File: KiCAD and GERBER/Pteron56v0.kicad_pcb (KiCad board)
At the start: 2 copper layers, 293.7 x 154 mm, 135 parts, among them SW1 SW_PUSH, SW10 SW_PUSH, SW11 SW_PUSH, SW12 SW_PUSH, SW13 SW_PUSH, SW14 SW_PUSH, SW15 SW_PUSH, SW16 SW_PUSH, SW17 SW_PUSH, SW18 SW_PUSH, SW19 SW_PUSH, SW2 SW_PUSH, SW20 SW_PUSH, SW21 SW_PUSH, SW22 SW_PUSH, SW23 SW_PUSH, SW24 SW_PUSH, SW25 SW_PUSH, SW26 SW_PUSH, SW27 SW_PUSH, SW28 SW_PUSH, SW29 SW_PUSH, SW3 SW_PUSH, SW30 SW_PUSH, SW31 SW_PUSH, SW32 SW_PUSH, SW33 SW_PUSH, SW34 SW_PUSH, SW35 SW_PUSH, SW36 SW_PUSH, SW37 SW_PUSH, SW38 SW_PUSH, SW39 SW_PUSH, SW4 SW_PUSH, SW40 SW_PUSH, SW41 SW_PUSH, SW42 SW_PUSH, SW43 SW_PUSH, SW44 SW_PUSH, SW45 SW_PUSH, SW46 SW_PUSH, SW47 SW_PUSH, SW48 SW_PUSH, SW49 SW_PUSH, SW5 SW_PUSH, SW50 SW_PUSH, SW51 SW_PUSH, SW52 SW_PUSH, SW53 SW_PUSH, SW54 SW_PUSH, SW55 SW_PUSH, SW56 SW_PUSH, SW6 SW_PUSH, SW7 SW_PUSH, SW8 SW_PUSH, SW9 SW_PUSH, U1 ProMicro

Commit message: add split wiring for standard Pteron56v0
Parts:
- removed D29, D30, D31, D32, D33, D34, D35, D36, D37, D38, D39, D40, D41, D42, D43, D44, D45, D46, D47, D48, D49, D50, D51, D52, D53, D54, D55, D56: 1N4148, Keyboard parts:D_DO-35_SOD27_P7.62mm_Horizontal
- removed G*** (x2): LOGO, Logos:PTERONsmaller
- removed G*** (x2): LOGO, Logos:bat56
- removed REF** (x18): MountingHole_2mm, MountingHole:MountingHole_2mm
- removed SW29, SW30, SW31, SW32, SW33, SW34, SW35, SW36, SW37, SW38, SW39, SW40, SW41, SW42, SW43, SW44, SW45, SW46, SW47, SW48, SW49, SW50, SW51, SW52, SW53, SW54, SW55, SW56: SW_PUSH, Keyboard parts:Mx_Alps_100
- added J1: AudioJack4, Connector_Audio:Jack_3.5mm_PJ320D_Horizontal, F.Cu at (105.9, 31.2)
- added J2: AudioJack4, Connector_Audio:Jack_3.5mm_PJ320D_Horizontal, B.Cu at (105.9, 31.2)
- D1, D10, D11, D12, D13, D14, D15, D16, D17, D18, D19, D2, D20, D21, D22, D23, D24, D25, D26, D27, D28, D3, D4, D5, D6, D7, D8, D9: footprint Keyboard parts:D_DO-35_SOD27_P7.62mm_Horizontal -> Keebio-Parts:Diode-dual
- SW1, SW10, SW11, SW12, SW13, SW14, SW15, SW16, SW17, SW18, SW19, SW2, SW20, SW21, SW22, SW23, SW24, SW25, SW26, SW27, SW28, SW3, SW4, SW5, SW6, SW7, SW8, SW9: footprint Keyboard parts:Mx_Alps_100 -> Keebio-Parts:Hybrid_PCB_100H_Dual_hole
- U1: footprint Keyboard parts:Pro_Micro -> promicro:ProMicro
- moved SW20 89.6 mm to (87.1, 128.9), turned to 37.5 degrees
- moved U1 86.9 mm to (159.5, 32.5)
- moved SW15 85.0 mm to (104.6, 118.4), turned to 25 degrees
- moved SW10 81.2 mm to (123.9, 111.7), turned to 12.5 degrees
- moved D28 78.8 mm to (112.0, 95.3), turned to 90 degrees
- moved SW5 78.5 mm to (144.2, 109.4), turned to 0 degrees
- moved SW28 76.7 mm to (121.5, 91.2), turned to 0 degrees
- moved D24 76.2 mm to (131.0, 93.9), turned to 90 degrees
- moved D5 76.0 mm to (165.8, 106.8), turned to 90 degrees
- moved D10 75.7 mm to (169.7, 106.8), turned to 90 degrees
- moved D15 75.4 mm to (173.6, 106.8), turned to 90 degrees
- moved D20 75.1 mm to (177.7, 106.8), turned to 90 degrees
- moved D27 74.5 mm to (111.9, 76.5), turned to 90 degrees
- moved SW24 74.0 mm to (140.5, 89.2), turned to 0 degrees
- moved D9 73.0 mm to (187.9, 101.2), turned to 90 degrees
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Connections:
- U1 pad 1: /Row0 -> (no net)
- U1 pad 10: /Col11 -> /Row2
- U1 pad 11: /Col10 -> /Row3
- U1 pad 19: Net-(U1-Pad19) -> (no net)
- U1 pad 2: /Row1 -> (no net)
- U1 pad 20: /Row2 -> (no net)
- U1 pad 21: Net-(U1-Pad21) -> (no net)
- U1 pad 22: Net-(U1-Pad22) -> (no net)
- U1 pad 23: Net-(U1-Pad23) -> (no net)
- U1 pad 24: Net-(U1-Pad24) -> (no net)
- U1 pad 3: Net-(U1-Pad3) -> (no net)
- U1 pad 4: Net-(U1-Pad4) -> (no net)
- U1 pad 5: /Col6 -> /Serial
- U1 pad 6: /Col7 -> (no net)
- U1 pad 7: /Row3 -> (no net)
- U1 pad 8: /Col8 -> /Row0
- U1 pad 9: /Col9 -> /Row1
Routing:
- net /Row1: track 403.7 -> 113.4 mm, vias 1 -> 0
- net /Row3: track 405.7 -> 146.7 mm, vias 2 -> 1
- net /Row0: track 377.4 -> 122.7 mm, vias 1 -> 0
- net /Row2: track 368.5 -> 135.1 mm, vias 0 -> 1
- net /Col11: track 202.1 -> 0.00 mm
- net /Col9: track 198.3 -> 0.00 mm, vias 1 -> 0
- net /Col8: track 190.0 -> 0.00 mm
- net /Col10: track 182.8 -> 0.00 mm
- net Net-(D41-Pad2): track 113.1 -> 0.00 mm
- net /Col7: track 112.5 -> 0.00 mm
- net /Col2: track 179.9 -> 83.0 mm, vias 1 -> 0
- net /Col6: track 86.7 -> 0.00 mm
- net Net-(D46-Pad2): track 85.3 -> 0.00 mm
- net /Row4: track 214.7 -> 137.8 mm, vias 0 -> 1
- net /Serial: track 0.00 -> 60.0 mm, vias 0 -> 1
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- added copper zone on B.Cu, net GND
- added copper zone on F.Cu, net VCC
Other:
- board size 293.7 x 154 mm -> 152.4 x 125.7 mm

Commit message: split36 version
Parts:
- removed D1, D2, D3, D4, D5: 1N4148, Keebio-Parts:Diode-dual
- removed SW1, SW2, SW3, SW4, SW5: SW_PUSH, Keebio-Parts:Hybrid_PCB_100H_Dual_hole
- moved D20 90.4 mm to (91.8, 135.1), turned to 217.5 degrees
- moved D15 68.0 mm to (108.2, 125.3), turned to 205 degrees
- moved D10 45.1 mm to (126.4, 119.5), turned to 192.5 degrees
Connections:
- U1 pad 14: /Col0 -> (no net)
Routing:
- net /Col0: track 163.0 -> 0.00 mm, vias 1 -> 0
- net Net-(D20-Pad2): track 102.6 -> 13.1 mm
- net /Col1: track 117.2 -> 191.9 mm
- net /Col2: track 83.0 -> 152.0 mm
- net Net-(D15-Pad2): track 79.8 -> 13.8 mm
- net /Col3: track 148.1 -> 191.5 mm
- net Net-(D10-Pad2): track 54.3 -> 12.7 mm
- net Net-(D5-Pad2): track 29.6 -> 0.00 mm
- net /Row3: track 146.7 -> 121.2 mm
- net /Row2: track 135.1 -> 111.3 mm
- net /Row1: track 113.4 -> 91.2 mm
- net /Row0: track 122.7 -> 104.9 mm
- net Net-(D4-Pad2): track 14.2 -> 0.00 mm
- net Net-(D1-Pad2): track 13.9 -> 0.00 mm
- net Net-(D2-Pad2): track 13.9 -> 0.00 mm
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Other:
- board size 152.4 x 125.7 mm -> 133.3 x 125.7 mm

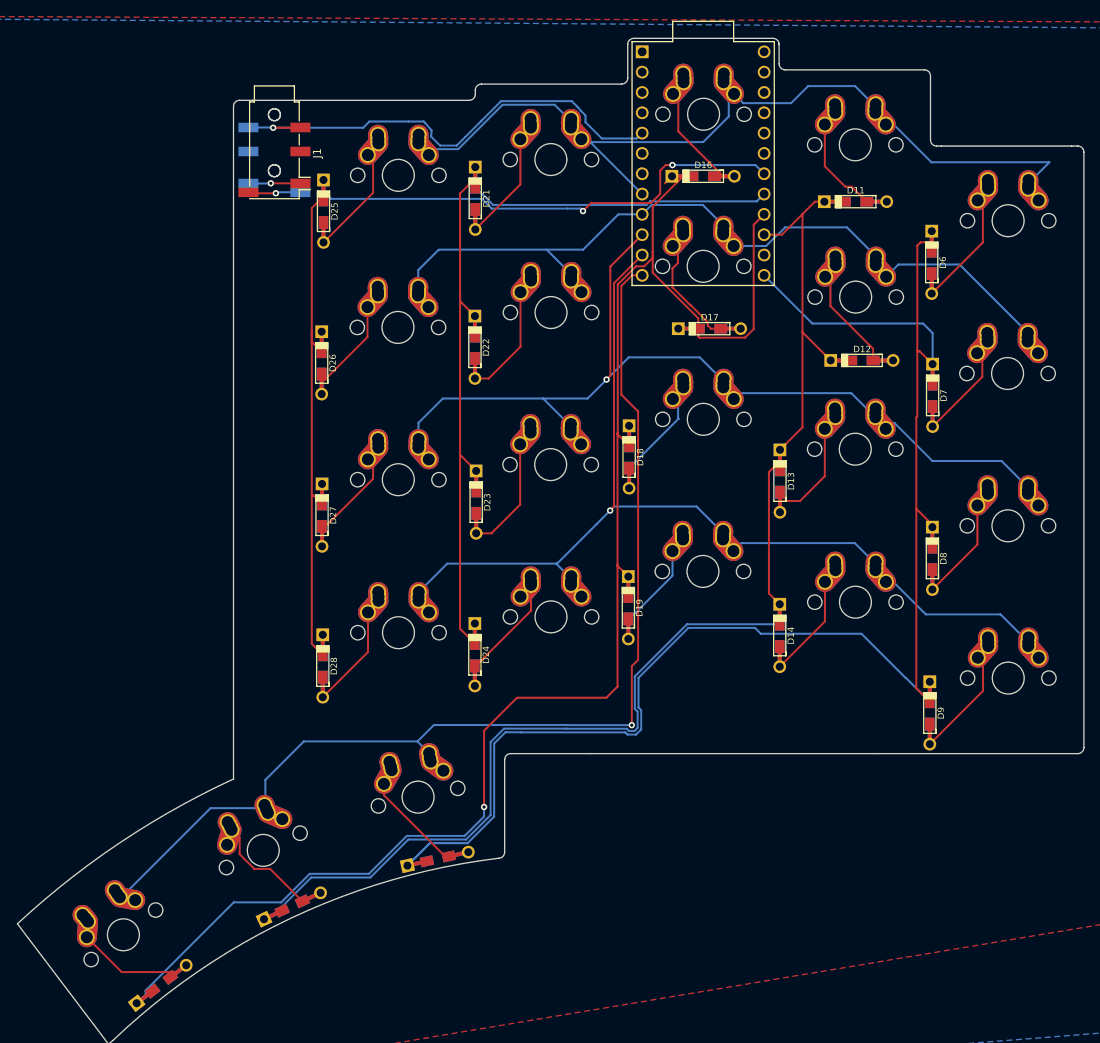
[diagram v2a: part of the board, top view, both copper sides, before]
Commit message: finalised the design, add mounting holes
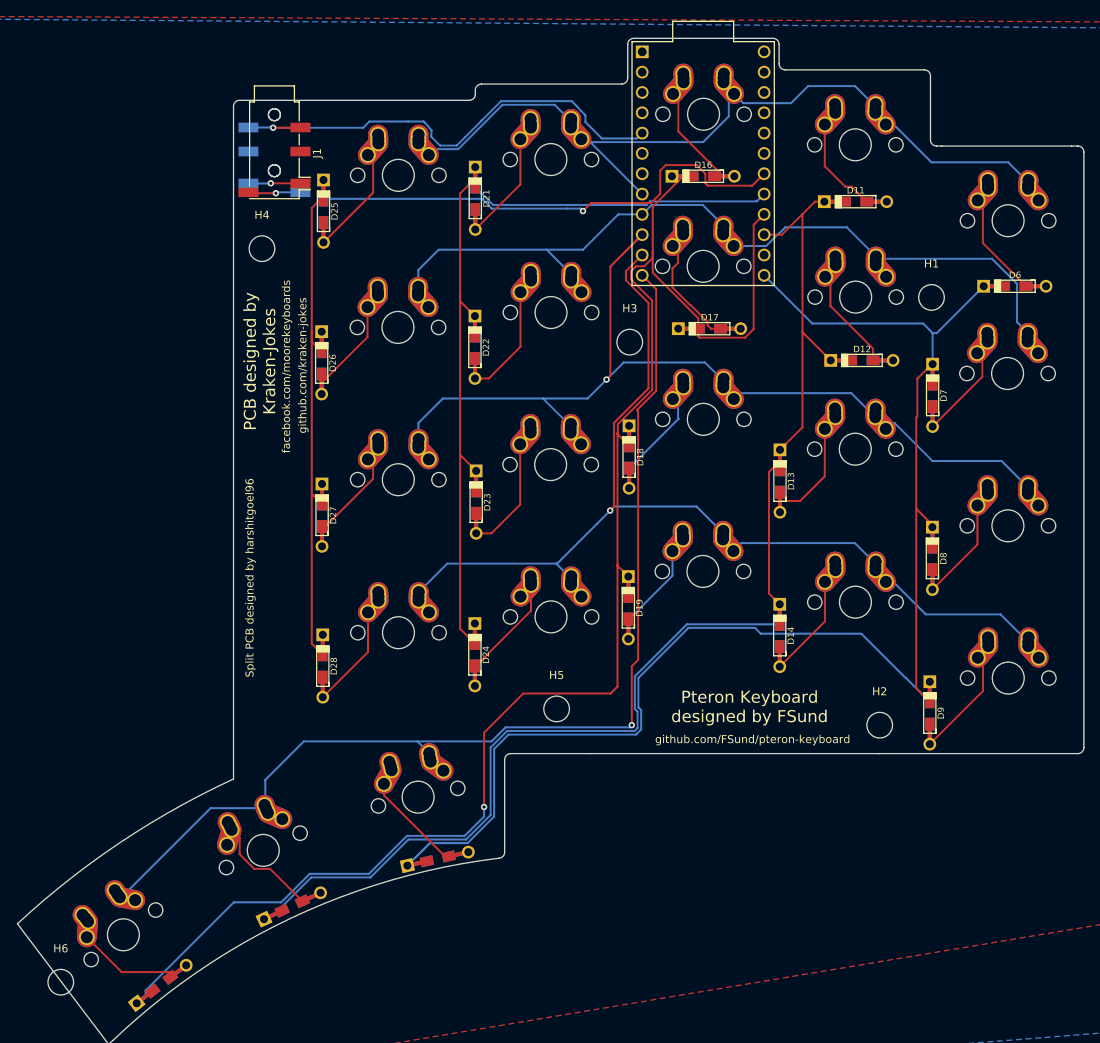
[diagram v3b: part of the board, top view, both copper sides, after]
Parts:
- added H1: MountingHole, MountingHole:MountingHole_3.2mm_M3, F.Cu at (188.1, 49.3)
- added H2: MountingHole, MountingHole:MountingHole_3.2mm_M3, F.Cu at (181.6, 102.7)
- added H3: MountingHole, MountingHole:MountingHole_3.2mm_M3, F.Cu at (150.4, 54.9)
- added H4: MountingHole, MountingHole:MountingHole_3.2mm_M3, F.Cu at (104.4, 43.2)
- added H5: MountingHole, MountingHole:MountingHole_3.2mm_M3, F.Cu at (141.2, 100.7)
- added H6: MountingHole, MountingHole:MountingHole_3.2mm_M3, F.Cu at (79.2, 134.9)
- moved D6 10.8 mm to (198.5, 47.9), turned to 180 degrees
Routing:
- net /Col1: track 191.9 -> 181.6 mm
- net /Row0: track 104.9 -> 99.7 mm
- net /Row1: track 91.2 -> 94.9 mm
- net /Row2: track 111.3 -> 114.3 mm
- net /Row3: track 121.2 -> 123.6 mm
- net /Col5: track 124.8 -> 126.7 mm, vias 2 -> 1
- net Net-(D6-Pad2): track 15.0 -> 13.7 mm
- net /Row4: track 136.9 -> 136.0 mm
- net /Col3: track 191.5 -> 192.3 mm
- net /Col2: track 152.0 -> 151.3 mm
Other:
- outline, holes or cut-outs redrawn
- board text added: "Split PCB designed by harshitgoel96"
- board text removed: "JLCJLCJLCJLC"
- board text removed: "Pteron56 PCB v0.2"

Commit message: small improvements
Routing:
- net /Col3: track 192.3 -> 181.1 mm
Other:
- board size 133.3 x 125.7 mm -> 136.1 x 127.1 mm
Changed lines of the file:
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@@
   (general
     (thickness 1.6)
-    (drawings 53)
-    (tracks 360)
+    (drawings 56)
+    (tracks 357)
     (zones 0)
     (modules 55)
@@
     (32 B.Adhes user hide)
     (33 F.Adhes user hide)
-    (34 B.Paste user)
+    (34 B.Paste user hide)
     (35 F.Paste user hide)
-    (36 B.SilkS user)
-    (37 F.SilkS user)
-    (38 B.Mask user)
-    (39 F.Mask user)
-    (40 Dwgs.User user)
-    (41 Cmts.User user)
+    (36 B.SilkS user hide)
+    (37 F.SilkS user hide)
+    (38 B.Mask user hide)
+    (39 F.Mask user hide)
+    (40 Dwgs.User user hide)
+    (41 Cmts.User user hide)
     (42 Eco1.User user hide)
     (43 Eco2.User user hide)
@@
     )
   )
+  (gr_line (start 71.082345 130.213421) (end 83.878669 144.009293) (layer Edge.Cuts) (width 0.05))
+  (gr_arc (start 144.1704 203.3397) (end 85.763282 142.153111) (angle -1.791806826) (layer Edge.Cuts) (width 0.05))
+  (gr_arc (start 144.145 203.3016) (end 73.826181 127.569855) (angle -2.11251843) (layer Edge.Cuts) (width 0.05))
+  (gr_line (start 104.557841 118.39453) (end 146.819667 209.025309) (layer Dwgs.User) (width 0.15))
+  (gr_line (start 87.074455 128.947849) (end 163.622035 228.706598) (layer Dwgs.User) (width 0.15))
   (gr_text github.com/kraken-jokes (at 109.474 57.785 90) (layer F.SilkS)
     (effects (font (size 1 1) (thickness 0.15)))
@@
   (gr_line (start 169.037 17.653) (end 169.037 20.066) (layer Edge.Cuts) (width 0.05))
   (gr_line (start 134.73 118.618) (end 134.73 117.983) (layer Edge.Cuts) (width 0.05))
-  (gr_line (start 85.217 142.621) (end 85.763281 142.15311) (layer Edge.Cuts) (width 0.05))
   (gr_arc (start 144.145 203.327) (end 133.968001 119.380001) (angle -36.7498178) (layer Edge.Cuts) (width 0.05))
   (gr_line (start 135.492 106.299) (end 145.542 106.299) (layer Edge.Cuts) (width 0.05))
@@
   (gr_arc (start 133.968 118.618) (end 133.968 119.38) (angle -90) (layer Edge.Cuts) (width 0.05))
   (gr_line (start 207.137 105.537) (end 207.137 31.115) (layer Edge.Cuts) (width 0.05))
-  (gr_line (start 73.82618 127.569854) (end 85.217 142.621) (layer Edge.Cuts) (width 0.05))
   (gr_line (start 100.838 101.727) (end 100.838 109.474) (layer Edge.Cuts) (width 0.05))
   (gr_arc (start 144.145 203.327) (end 100.838001 109.474001) (angle -18.09767132) (layer Edge.Cuts) (width 0.05))
@@
   (segment (start 148.844 82.817585) (end 150.192403 84.165988) (width 0.25) (layer F.Cu) (net 13))
   (segment (start 148.844 82.677) (end 148.844 82.817585) (width 0.25) (layer F.Cu) (net 13))
-  (segment (start 167.16375 38.89375) (end 165.862 40.1955) (width 0.25) (layer F.Cu) (net 13))
-  (segment (start 164.777501 54.306251) (end 159.081251 54.306251) (width 0.25) (layer F.Cu) (net 13))
-  (segment (start 165.862 53.221752) (end 164.777501 54.306251) (width 0.25) (layer F.Cu) (net 13))
-  (segment (start 165.862 40.1955) (end 165.862 53.221752) (width 0.25) (layer F.Cu) (net 13))
-  (segment (start 158.9375 54.1625) (end 158.9375 53.18125) (width 0.25) (layer F.Cu) (net 13))
-  (segment (start 159.081251 54.306251) (end 158.9375 54.1625) (width 0.25) (layer F.Cu) (net 13))
   (segment (start 157.04375 34.13125) (end 153.240523 37.934477) (width 0.25) (layer F.Cu) (net 13))
   (segment (start 158.9375 51.8765) (end 158.9375 53.18125) (width 0.25) (layer F.Cu) (net 13))
@@
   (segment (start 148.8694 65.12419) (end 148.8694 66.19494) (width 0.25) (layer F.Cu) (net 13))
   (segment (start 153.162 60.83159) (end 148.8694 65.12419) (width 0.25) (layer F.Cu) (net 13))
+  (segment (start 157.04375 34.13125) (end 158.66851 35.75601) (width 0.25) (layer F.Cu) (net 13))
+  (segment (start 164.02601 35.75601) (end 167.16375 38.89375) (width 0.25) (layer F.Cu) (net 13))
+  (segment (start 158.66851 35.75601) (end 164.02601 35.75601) (width 0.25) (layer F.Cu) (net 13))
   (segment (start 156.437436 28.524936) (end 162.04375 34.13125) (width 0.25) (layer F.Cu) (net 14))
   (segment (start 156.437436 23.108156) (end 156.437436 28.524936) (width 0.25) (layer F.Cu) (net 14))

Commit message: added gerber files
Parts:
- added H7: MountingHole, MountingHole:MountingHole_3.2mm_M3, F.Cu at (106.0, 103.0)

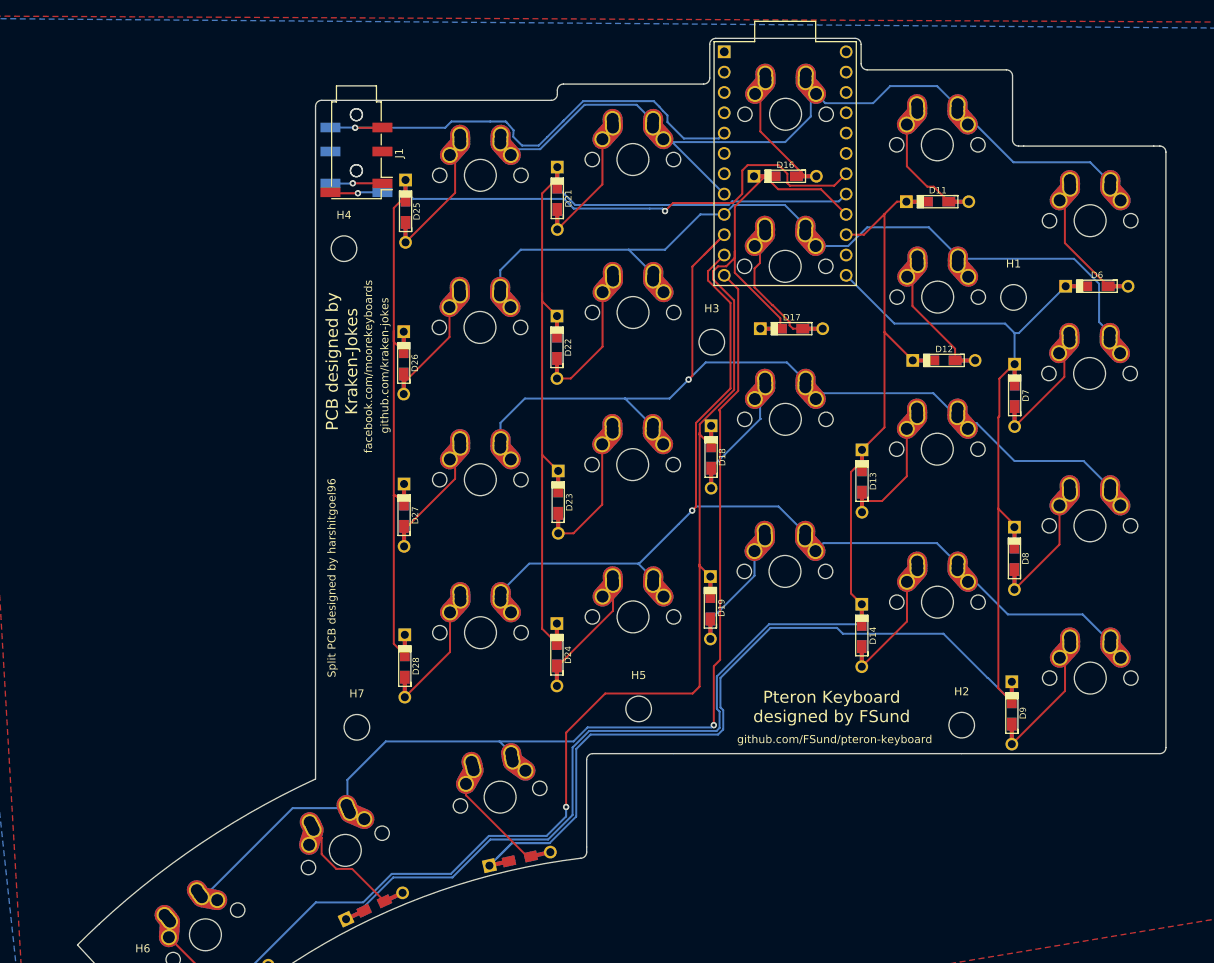
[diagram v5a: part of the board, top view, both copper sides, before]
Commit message: remove top row.
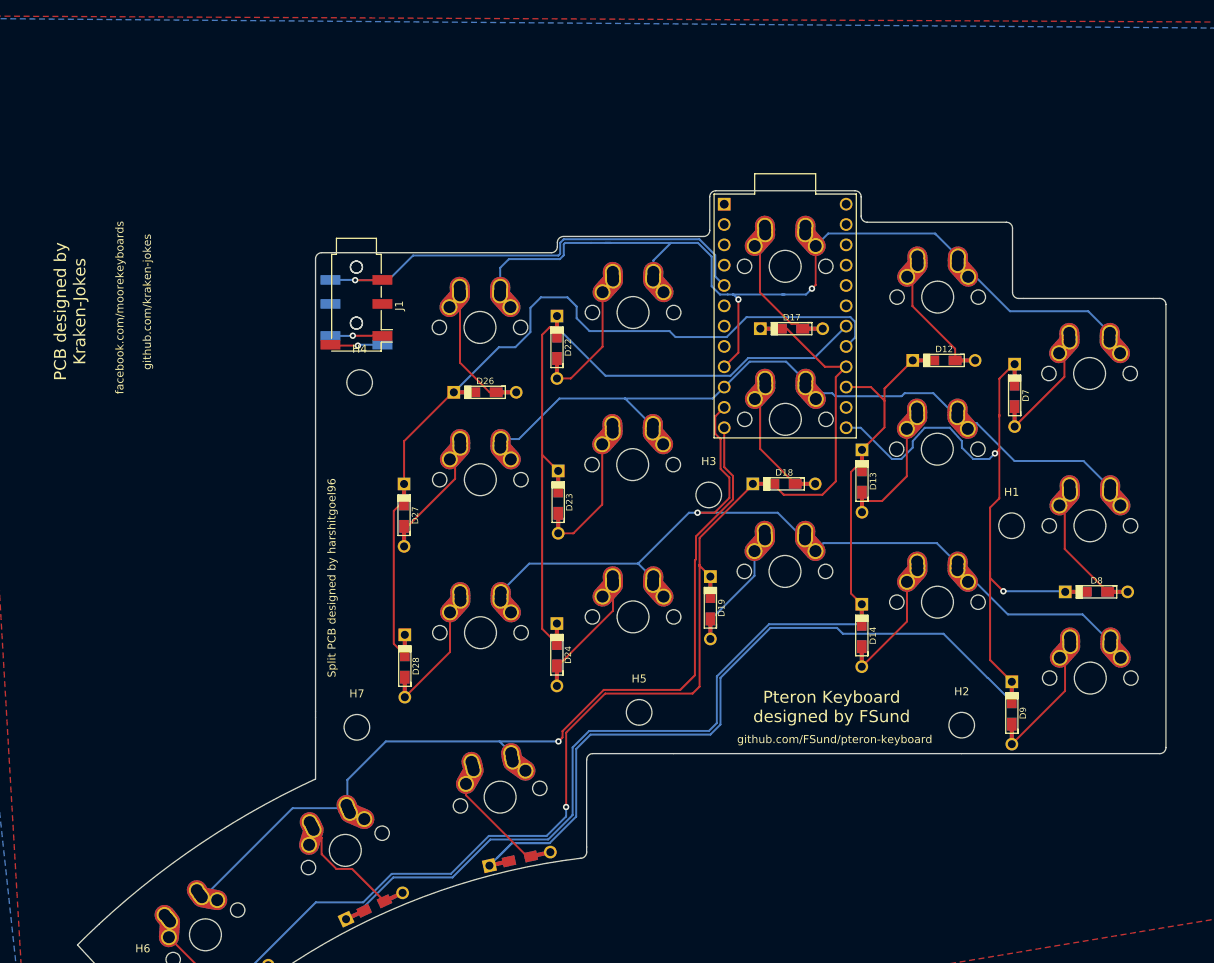
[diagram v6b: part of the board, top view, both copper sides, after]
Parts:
- removed D11, D16, D21, D25, D6: 1N4148, Keebio-Parts:Diode-dual
- removed SW11, SW16, SW21, SW25, SW6: SW_PUSH, Keebio-Parts:Hybrid_PCB_100H_Dual_hole
- moved H1 28.5 mm to (187.8, 77.8)
- moved H3 19.1 mm to (150.0, 74.0)
- moved J1 19.1 mm to (105.9, 50.3)
- moved J2 19.1 mm to (105.9, 50.3)
- moved U1 19.0 mm to (159.5, 51.6)
- moved H4 16.9 mm to (106.3, 59.9)
- moved D8 11.1 mm to (198.5, 86.1), turned to 180 degrees
- moved D26 10.8 mm to (122.0, 61.1), turned to 180 degrees
- moved D18 9.71 mm to (159.4, 72.6), turned to 180 degrees
- moved H5 0.44 mm to (141.3, 101.1)
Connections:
- U1 pad 17: /Col4 -> /Col5
- U1 pad 18: /Col5 -> /Col4
- U1 pad 8: /Row0 -> (no net)
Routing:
- net /Row0: track 99.7 -> 0.00 mm
- net /Col3: track 181.1 -> 147.0 mm
- net /Col5: track 126.7 -> 99.8 mm, vias 1 -> 0
- net /Col2: track 151.3 -> 124.9 mm
- net /Row2: track 114.3 -> 89.7 mm, vias 1 -> 0
- net /Row4: track 136.0 -> 111.7 mm
- net /Col4: track 103.8 -> 85.7 mm
- net /Row3: track 123.6 -> 105.7 mm
- net /Row1: track 94.9 -> 111.2 mm, vias 0 -> 2
- net Net-(D25-Pad2): track 14.2 -> 0.00 mm
- net Net-(D6-Pad2): track 13.7 -> 0.00 mm
- net Net-(D21-Pad2): track 13.6 -> 0.00 mm
- net Net-(D16-Pad2): track 13.3 -> 0.00 mm
- net Net-(D11-Pad2): track 12.3 -> 0.00 mm
- net /Col1: track 181.6 -> 175.8 mm, vias 0 -> 2
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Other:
- board size 136.1 x 127.1 mm -> 136.1 x 108.1 mm
